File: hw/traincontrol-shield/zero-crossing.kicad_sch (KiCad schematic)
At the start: 3 parts, among them U2 H11AA1

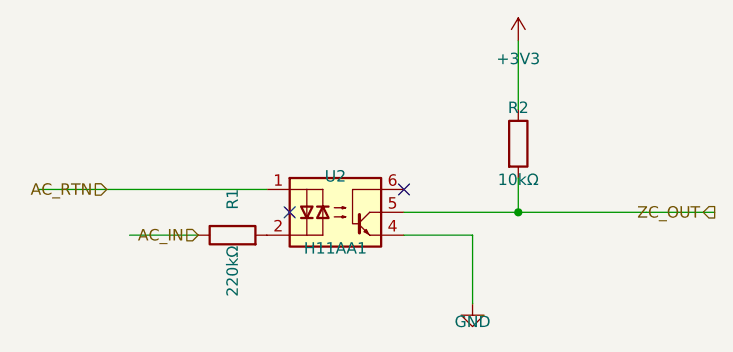
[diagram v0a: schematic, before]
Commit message: Revert "Fix hierarchical label orientations: angle=0 → angle=180 throughout"
This reverts commit 593a08d7401abe541600d63447176c71f07219f1.
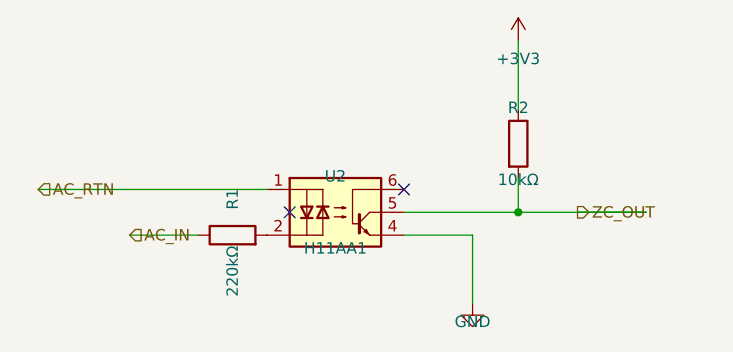
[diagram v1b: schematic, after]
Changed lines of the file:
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@@
 	(hierarchical_label "AC_IN"
 		(shape input)
-		(at 81.28 92.71 180)
+		(at 73.66 92.71 0)
 		(fields_autoplaced yes)
-		(effects (font (size 1.27 1.27)) (justify right bottom))
+		(effects (font (size 1.27 1.27)) (justify left bottom))
 		(property "Intersheetrefs" "${INTERSHEET_REFS}"
-			(at 81.28 92.71 0)
+			(at 73.66 92.71 0)
 			(effects (font (size 1.27 1.27)) (hide yes))
 		)
 	)
 	(wire
-		(pts (xy 63.5 87.63) (xy 71.12 87.63))
+		(pts (xy 63.50000000000001 87.63) (xy 71.12 87.63))
 		(stroke (width 0) (type solid))
 	)
 	(hierarchical_label "AC_RTN"
 		(shape input)
-		(at 71.12 87.63 180)
+		(at 63.50000000000001 87.63 0)
 		(fields_autoplaced yes)
-		(effects (font (size 1.27 1.27)) (justify right bottom))
+		(effects (font (size 1.27 1.27)) (justify left bottom))
 		(property "Intersheetrefs" "${INTERSHEET_REFS}"
-			(at 71.12 87.63 0)
+			(at 63.50000000000001 87.63 0)
 			(effects (font (size 1.27 1.27)) (hide yes))
 		)
 	)
 	(wire
-		(pts (xy 131.04 90.17) (xy 138.66 90.17))
+		(pts (xy 123.41999999999999 90.17) (xy 131.04 90.17))
 		(stroke (width 0) (type solid))
 	)
 	(hierarchical_label "ZC_OUT"
 		(shape output)
-		(at 138.66 90.17 180)
+		(at 123.41999999999999 90.17 0)
 		(fields_autoplaced yes)
-		(effects (font (size 1.27 1.27)) (justify right bottom))
+		(effects (font (size 1.27 1.27)) (justify left bottom))
 		(property "Intersheetrefs" "${INTERSHEET_REFS}"
-			(at 138.66 90.17 0)
+			(at 123.41999999999999 90.17 0)
 			(effects (font (size 1.27 1.27)) (hide yes))
 		)
